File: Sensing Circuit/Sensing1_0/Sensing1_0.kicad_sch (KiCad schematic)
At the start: 41 parts, among them J1 Conn_02x14_Odd_Even, Q1 NPN, Q2 NPN

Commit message: Sensing Circuit KiCaD files updated
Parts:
- removed D4, D6: PhotoDiode, LED_THT:LED_D5.0mm_Horizontal_O1.27mm_Z3.0mm, symbol Sensor_Optical:SFH205F
- removed D8, D9: LED, LED_THT:LED_SideEmitter_Rectangular_W4.5mm_H1.6mm, symbol LED:TSAL4400
- added D4, D6: LED, LED_THT:LED_D5.0mm_Horizontal_O1.27mm_Z15.0mm, symbol LED:TSAL4400
- added D8, D9: PhotoDiode, LED_THT:LED_D5.0mm_Horizontal_O1.27mm_Z15.0mm, symbol Sensor_Optical:SFH205F
- added JP10, JP11, JP12, JP13, JP14, JP15, JP7, JP8, JP9: SJ_Open, Jumper:SolderJumper-2_P1.3mm_Open_RoundedPad1.0x1.5mm, symbol Jumper:SolderJumper_2_Open
- added R19, R21: 4.7k, Resistor_SMD:R_0603_1608Metric, symbol Device:R
- added R20: 10k, Resistor_SMD:R_0603_1608Metric, symbol Device:R
- D1, D2, D3, D7: footprint LED_THT:LED_SideEmitter_Rectangular_W4.5mm_H1.6mm -> LED_THT:LED_D5.0mm_Horizontal_O1.27mm_Z15.0mm; LCSC (none) -> C55528
- D5: footprint LED_THT:LED_D5.0mm_Horizontal_O1.27mm_Z3.0mm -> LED_THT:LED_D5.0mm_Horizontal_O1.27mm_Z15.0mm; LCSC (none) -> C2900211
- J1: footprint (none) -> Connector_PinSocket_2.54mm:PinSocket_2x14_P2.54mm_Vertical
- JP1, JP2, JP3, JP4, JP5, JP6: footprint (none) -> Jumper:SolderJumper-2_P1.3mm_Open_RoundedPad1.0x1.5mm
- Q1, Q2: footprint (none) -> Package_TO_SOT_SMD:SOT-23; LCSC (none) -> C2145
- R1, R2, R4: value 27 -> 22; footprint (none) -> Resistor_SMD:R_0603_1608Metric; LCSC (none) -> C23345
- R10: value 10k -> 100; footprint (none) -> Resistor_SMD:R_0603_1608Metric; LCSC (none) -> C22775
- R11: value 50k -> 75; footprint (none) -> Resistor_SMD:R_0603_1608Metric; LCSC (none) -> C4275
- R12: value 10k -> 22; footprint (none) -> Resistor_SMD:R_0603_1608Metric; LCSC (none) -> C23345
- R13: value 150 -> 22; footprint (none) -> Resistor_SMD:R_0603_1608Metric; LCSC (none) -> C23345
- R14: value 100 -> 22; footprint (none) -> Resistor_SMD:R_0603_1608Metric; LCSC (none) -> C23345
- R15: value 75 -> 47k; footprint (none) -> Resistor_SMD:R_0603_1608Metric; LCSC (none) -> C25819
- R16: value 27 -> 10k; footprint (none) -> Resistor_SMD:R_0603_1608Metric; LCSC (none) -> C25804
- R17: value 27 -> 4.7k; footprint (none) -> Resistor_SMD:R_0603_1608Metric; LCSC (none) -> C23162
- R18: value 27 -> 47k; footprint (none) -> Resistor_SMD:R_0603_1608Metric; LCSC (none) -> C25819
- R3: footprint (none) -> Resistor_SMD:R_0603_1608Metric; LCSC (none) -> C22808
- R5: value 50k -> 150; footprint (none) -> Resistor_SMD:R_0603_1608Metric; LCSC (none) -> C22808
- R6: footprint (none) -> Resistor_SMD:R_0603_1608Metric; LCSC (none) -> C22775
- R7: value 50k -> 47k; footprint (none) -> Resistor_SMD:R_0603_1608Metric; LCSC (none) -> C25819
- R8: footprint (none) -> Resistor_SMD:R_0603_1608Metric; LCSC (none) -> C25804
- R9: footprint (none) -> Resistor_SMD:R_0603_1608Metric; LCSC (none) -> C4275
- TP1, TP2, TP3, TP4, TP5: footprint (none) -> TestPoint:TestPoint_Pad_1.5x1.5mm
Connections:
- net PA14 is gone; now on net PE14: J1.10 (Pin_10)
- net PE15 is gone; now on net PE13: JP1.2 (B), R3.1
- net +BATT: now also D4.2 (A), D6.2 (A), D8.1 (K), D9.1 (K)
- net GND: now also R17.2, JP12.1 (A), JP15.1 (A), JP9.1 (A), R19.2, R21.2; no longer R10.2, R12.2, R8.2
- net PA3: now also JP7.2 (B)
- net PA4: now also R15.1, TP4.1, D8.2 (A), JP10.2 (B); no longer R5.1, TP3.1
- net PA5: now also R18.1, TP5.1, D9.2 (A), JP13.2 (B); no longer R11.1, TP4.1
- net PE14: now also R5.1; no longer R13.1
- net at R17.1: now also R16.2, JP11.1 (A), JP12.2 (B)
- net at R11.2: now also JP6.1 (A), Q2.2 (B), TP3.1; no longer R12.1
- net at JP5.1 (A), JP6.2 (B): now also R10.2, R11.1; no longer R14.2, R15.1
- net at JP4.1 (A), JP5.2 (B): now also R10.1, R5.2; no longer R13.2, R14.1
- net at D7.1 (K): now also R14.1; no longer R16.1
- net PE13: now reaches J1.12 (Pin_12)
- net at R7.2, R8.1: now also JP7.1 (A), JP8.2 (B)
- net PA15: no longer names the net of J1.8 (Pin_8)
- new net: JP14.1 (A), JP15.2 (B), R20.2, R21.1
- new net: JP13.1 (A), JP14.2 (B), R18.2, R20.1
- new net: Q2.1 (C), R12.2, R13.2, R14.2
- new net: D6.1 (K), R13.1
- new net: D4.1 (K), R12.1
- new net: JP10.1 (A), JP11.2 (B), R15.2, R16.1
- new net: JP8.1 (A), JP9.2 (B), R19.1, R8.2
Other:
- moved on the sheet: D1, D2, D3, JP1, JP2, JP3, Q1, R1, R2, R3, R4, R6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

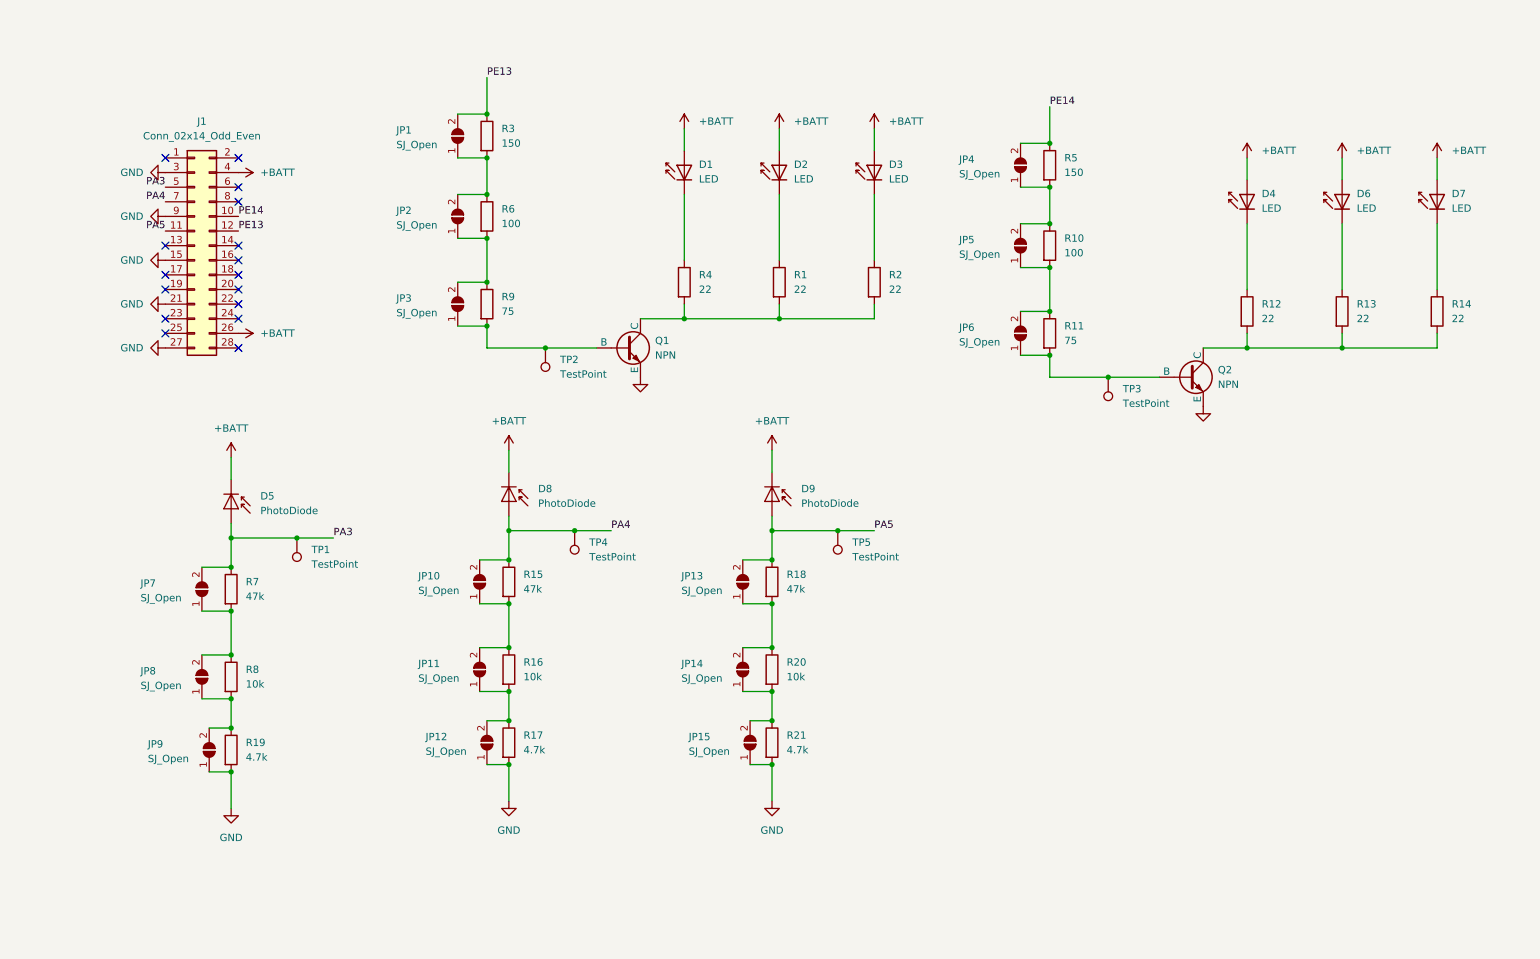
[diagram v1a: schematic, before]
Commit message: Sensig circuit schematic files updated, Datasheets added, Schematic and PCB figures added and interim report added.
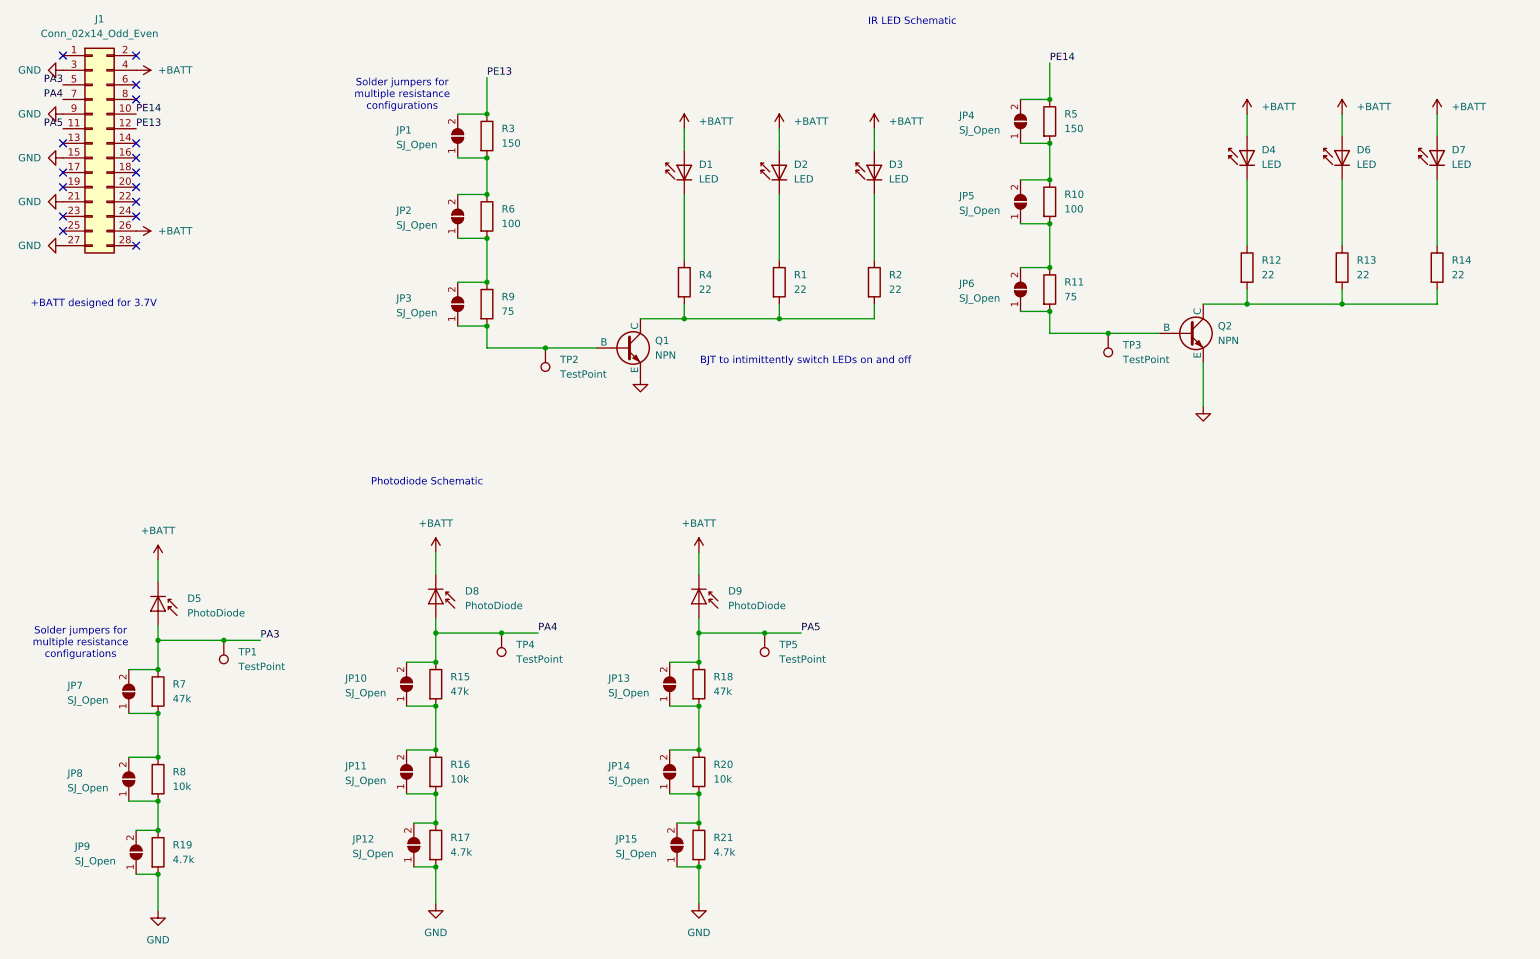
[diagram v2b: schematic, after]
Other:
- note added: "+BATT designed for 3.7V"
- note added: "BJT to intimittently switch LEDs on and off"
- note added: "IR LED Schematic"
- note added: "Photodiode Schematic"
- note added: "Solder jumpers for multiple resistance configurations"
- company: (none) -> University of Cape Town
- title: (none) -> Sensing Subsystem For Micro-Mouse
- moved on the sheet: D4, D5, D6, D7, D8, D9, J1, JP10, JP11, JP12, JP13, JP14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
